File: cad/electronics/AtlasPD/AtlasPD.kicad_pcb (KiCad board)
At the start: 2 copper layers, 12 parts, among them J1 Conn_01x02_Male, J2 Conn_01x02_Male, U1 LM2678T-ADJ_NOPB

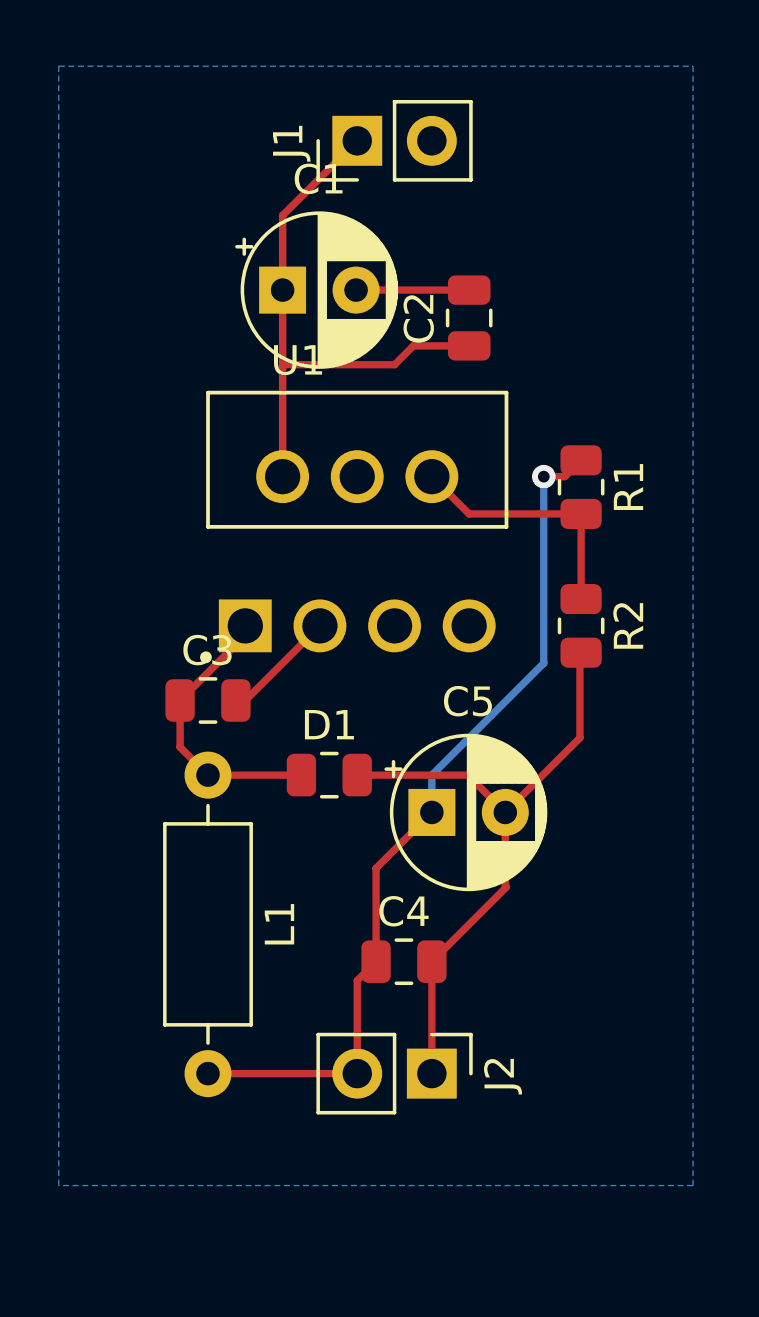
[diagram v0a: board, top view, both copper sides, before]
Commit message: Finished Basic Buck Converter Design
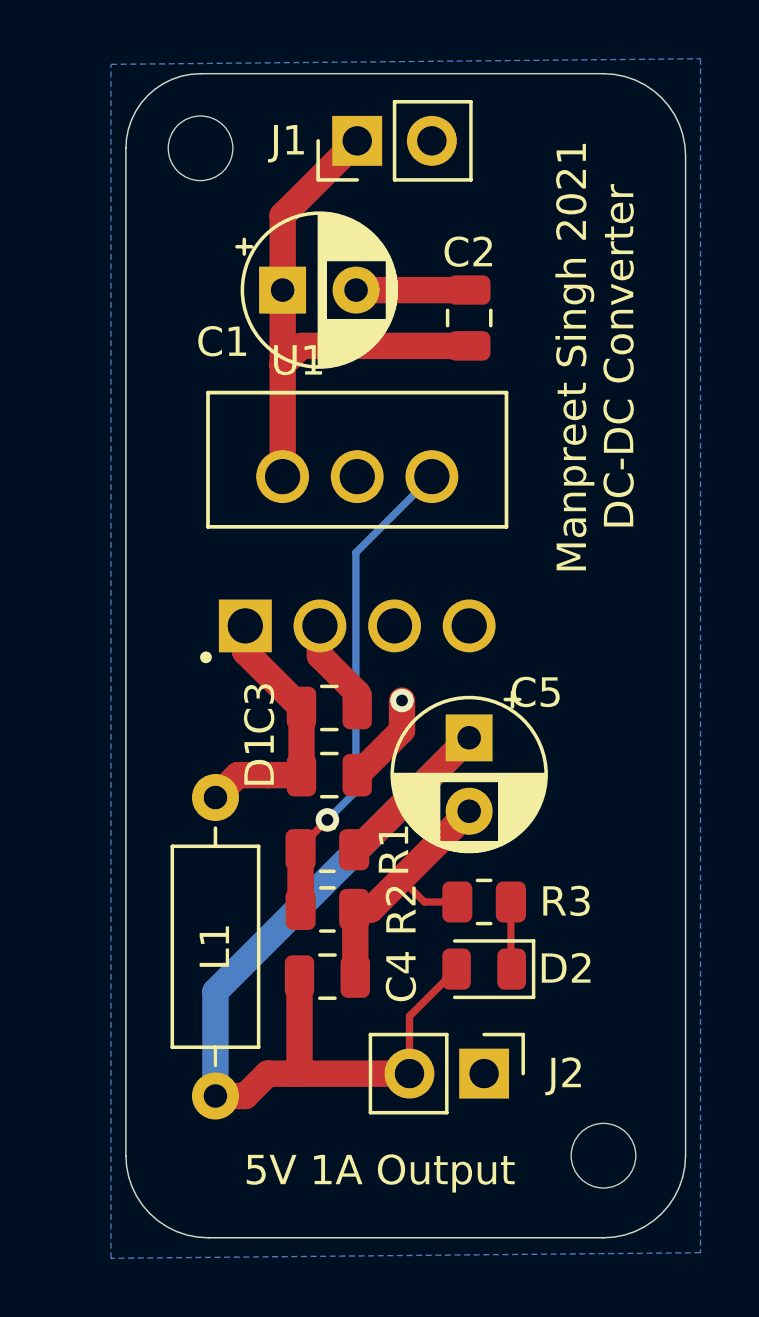
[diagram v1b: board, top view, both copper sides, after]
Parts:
- added D2: LED, LED_SMD:LED_0805_2012Metric, F.Cu at (42.4, 42.2)
- added R3: 1k, Resistor_SMD:R_0805_2012Metric, F.Cu at (42.4, 39.9)
- added REF**: MountingHole_2.2mm_M2_DIN965, MountingHole:MountingHole_2.2mm_M2_DIN965, F.Cu at (46.5, 48.5)
- added REF**: MountingHole_2.2mm_M2_DIN965, MountingHole:MountingHole_2.2mm_M2_DIN965, F.Cu at (32.8, 14.2)
- moved R1 15.1 mm to (37.1, 38.1), turned to 180 degrees
- moved R2 13.0 mm to (37.1, 40.1), turned to 0 degrees
- moved C3 4.14 mm to (37.1, 33.3)
- moved C5 2.84 mm to (41.9, 34.3), turned to 270 degrees
- moved C4 2.66 mm to (37.1, 42.4)
- moved J2 1.78 mm to (42.4, 45.7)
- moved L1 0.80 mm to (33.3, 36.3)
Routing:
- net GND: track 25.9 -> 16.8 mm, vias 0 -> 1
- net Net-(R1-Pad2): track 8.50 -> 16.6 mm, vias 0 -> 1
- net Net-(C4-Pad1): track 29.5 -> 35.7 mm, vias 1 -> 0
- net Net-(D2-Pad1): track 0.00 -> 2.30 mm
- net Net-(C3-Pad2): track 3.91 -> 3.32 mm
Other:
- board outline added: 19.1 x 39.6 mm
- board text added: "5V 1A Output"
- board text added: "Manpreet Singh 2021 DC-DC Converter"

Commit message: Pushing latest changes
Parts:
- added U2: NUCLEO-L432KC, NUCLEO-L432KC:MODULE_NUCLEO-L432KC, F.Cu at (80.5, 40.4)
- moved REF** 27.8 mm to (22.6, 34.3), turned to 270 degrees
- moved REF** 25.0 mm to (56.9, 20.6), turned to 270 degrees
- moved J2 23.0 mm to (25.4, 30.2), turned to 180 degrees
- moved J1 22.5 mm to (57.1, 25.9), turned to 0 degrees
- moved C4 19.4 mm to (28.7, 24.9), turned to 270 degrees
- moved D2 18.0 mm to (29.0, 30.2), turned to 90 degrees
- moved C1 17.1 mm to (52.1, 23.4), turned to 270 degrees
- moved R2 16.4 mm to (31.0, 24.9), turned to 270 degrees
- moved L1 15.3 mm to (34.8, 21.1), turned to 180 degrees
- moved R3 14.8 mm to (31.2, 30.2), turned to 90 degrees
- moved R1 13.8 mm to (33.0, 24.9), turned to 90 degrees
- moved C2 13.4 mm to (51.1, 29.7), turned to 0 degrees
- moved D1 10.7 mm to (35.6, 25.0), turned to 270 degrees
- moved C3 8.35 mm to (37.8, 25.0), turned to 270 degrees
- moved U1 7.64 mm to (45.7, 25.9), turned to 270 degrees
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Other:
- board size 19.1 x 39.6 mm -> 39.6 x 19.1 mm

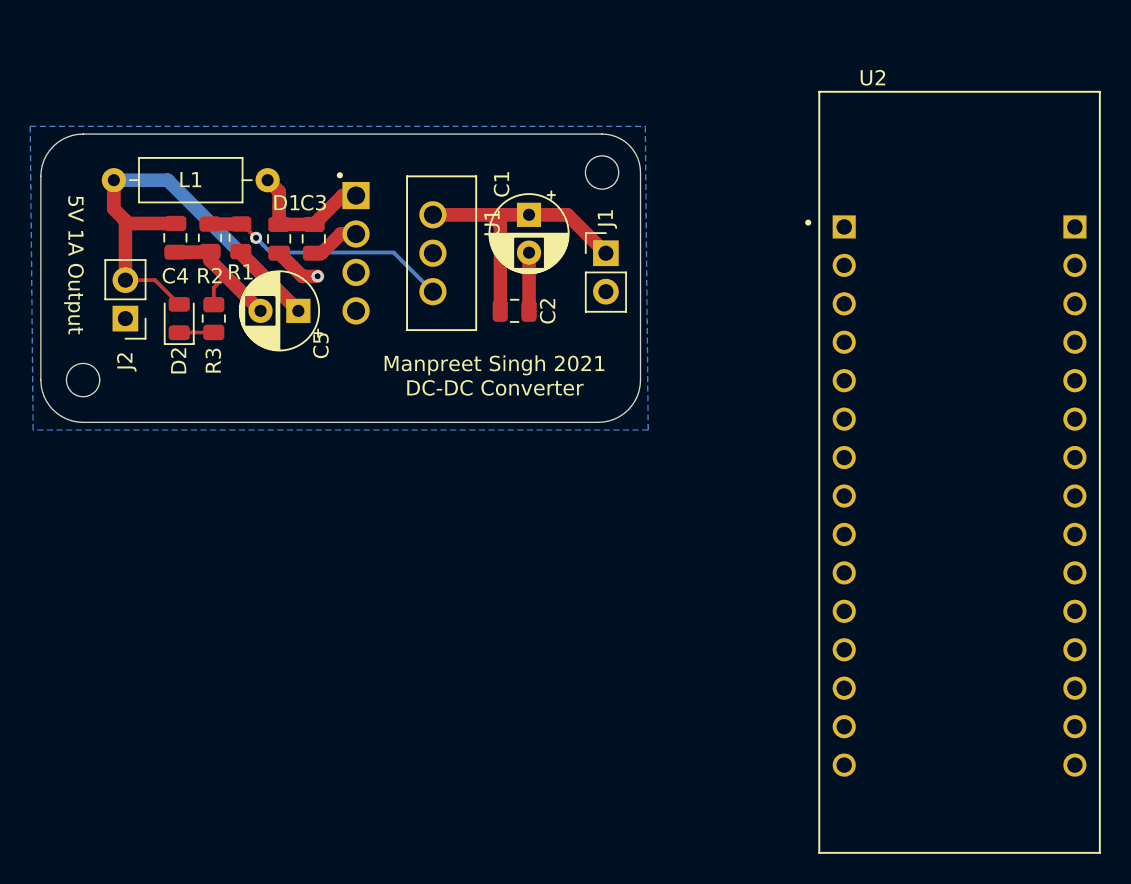
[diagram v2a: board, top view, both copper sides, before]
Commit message: PCB Changes to 5V Regulator
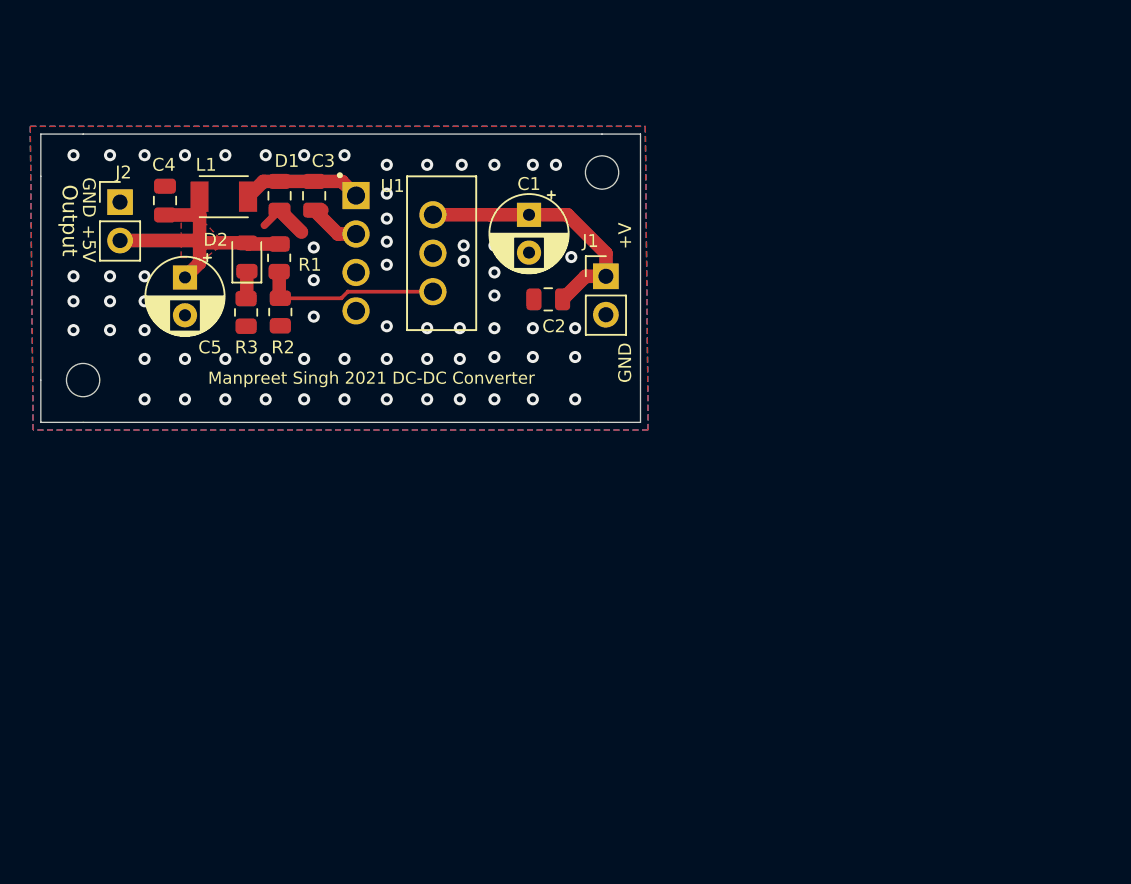
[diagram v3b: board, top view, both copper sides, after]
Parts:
- removed U2: NUCLEO-L432KC, NUCLEO-L432KC:MODULE_NUCLEO-L432KC
- L1: footprint Inductor_THT:L_Axial_L6.6mm_D2.7mm_P10.16mm_Horizontal_Vishay_IM-2 -> Inductor_SMD:L_TDK_NLV32_3.2x2.5mm
- moved C5 7.81 mm to (29.3, 27.5), turned to 270 degrees
- moved J2 7.70 mm to (25.0, 22.5), turned to 0 degrees
- moved R2 6.76 mm to (35.6, 29.8)
- moved D2 6.04 mm to (33.4, 26.2)
- moved L1 3.09 mm to (31.9, 22.2)
- moved R1 2.86 mm to (35.6, 26.2), turned to 270 degrees
- moved C3 2.84 mm to (37.9, 22.1)
- moved D1 2.84 mm to (35.6, 22.1)
- moved C4 2.56 mm to (28.0, 22.4), turned to 90 degrees
- moved C2 2.35 mm to (53.3, 29.0), turned to 180 degrees
- moved R3 2.17 mm to (33.4, 29.8), turned to 270 degrees
- moved J1 1.52 mm to (57.1, 27.4)
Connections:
- net Net-(C4-Pad1) renamed /Sheet60A23886/Output
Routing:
- net /Sheet60A23886/Output: track 35.7 -> 18.6 mm
- net GND: track 16.8 -> 3.47 mm, vias 1 -> 66
- net Net-(R1-Pad2): track 16.6 -> 12.1 mm, vias 1 -> 0
- net Net-(C1-Pad1): track 19.1 -> 17.5 mm
- net Net-(C3-Pad1): track 9.11 -> 7.94 mm
- net Net-(C3-Pad2): track 3.32 -> 3.93 mm
- added copper zone on F.Cu, net /Sheet60A23886/Output
- added copper zone on F.Cu, net GND
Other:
- outline, holes or cut-outs redrawn
- board text added: "+5V"
- board text added: "+V"
- board text added: "GND"
- board text added: "JLCJLCJLCJLC"
- board text added: "Output"
- board text removed: "5V 1A Output"

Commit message: More PCB changes
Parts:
- D1: footprint Capacitor_SMD:C_0805_2012Metric -> Diode_SMD:D_SOD-128
- moved D2 6.30 mm to (32.3, 32.4), turned to 180 degrees
- moved R3 3.74 mm to (36.1, 32.4), turned to 0 degrees
- moved L1 3.67 mm to (33.9, 25.2)
- moved C3 3.32 mm to (37.8, 25.4)
- moved R1 2.45 mm to (34.7, 28.5), turned to 0 degrees
- moved J2 2.28 mm to (27.0, 21.3)
- moved R2 2.26 mm to (37.8, 29.2)
- moved REF** 2.24 mm to (24.8, 34.3)
- moved C4 2.08 mm to (30.1, 22.1)
- moved C5 0.48 mm to (28.9, 27.5)
- moved D1 0.20 mm to (35.6, 21.9), turned to 180 degrees
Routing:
- net /Sheet60A23886/Output: track 18.6 -> 20.9 mm
- net Net-(R1-Pad2): track 12.1 -> 10.2 mm
- net GND: track 3.47 -> 2.56 mm, vias 66 -> 31
- removed copper zone on F.Cu, net /Sheet60A23886/Output
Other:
- board size 39.6 x 19.1 mm -> 37.4 x 19.1 mm

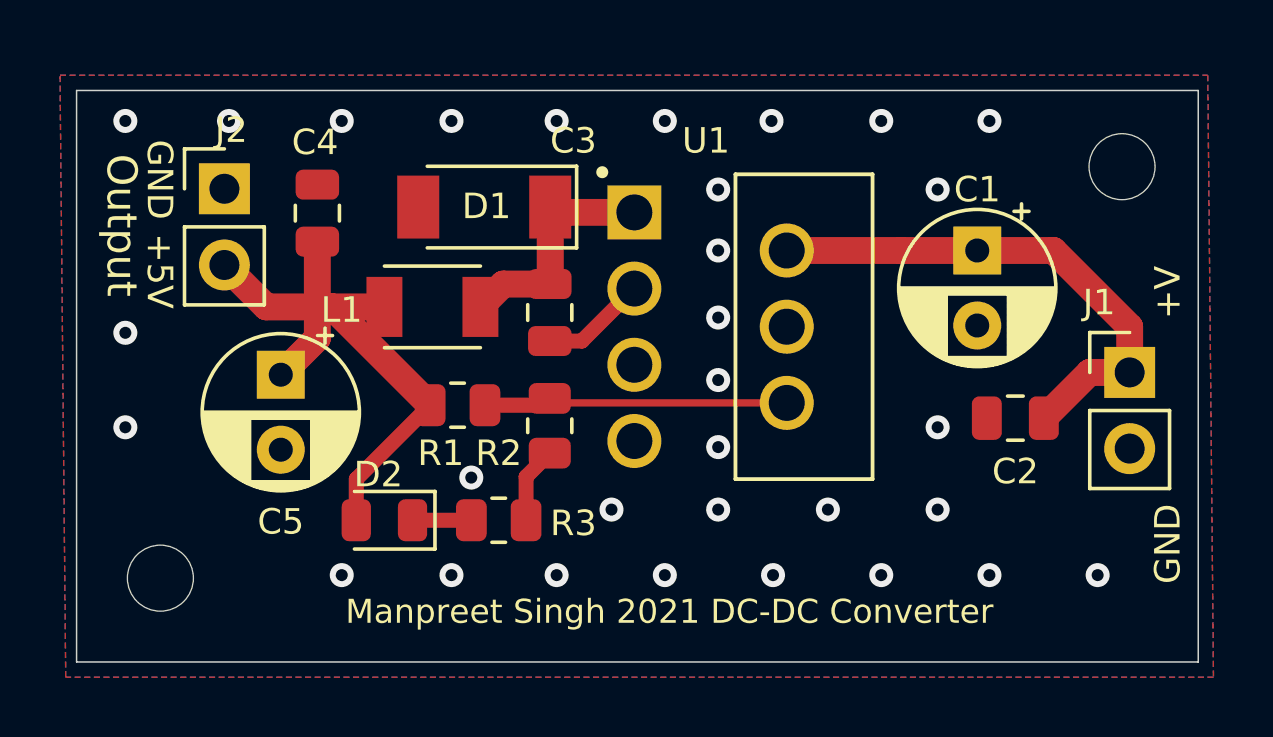
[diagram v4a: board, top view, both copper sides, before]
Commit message: Prep for short run production of power converter
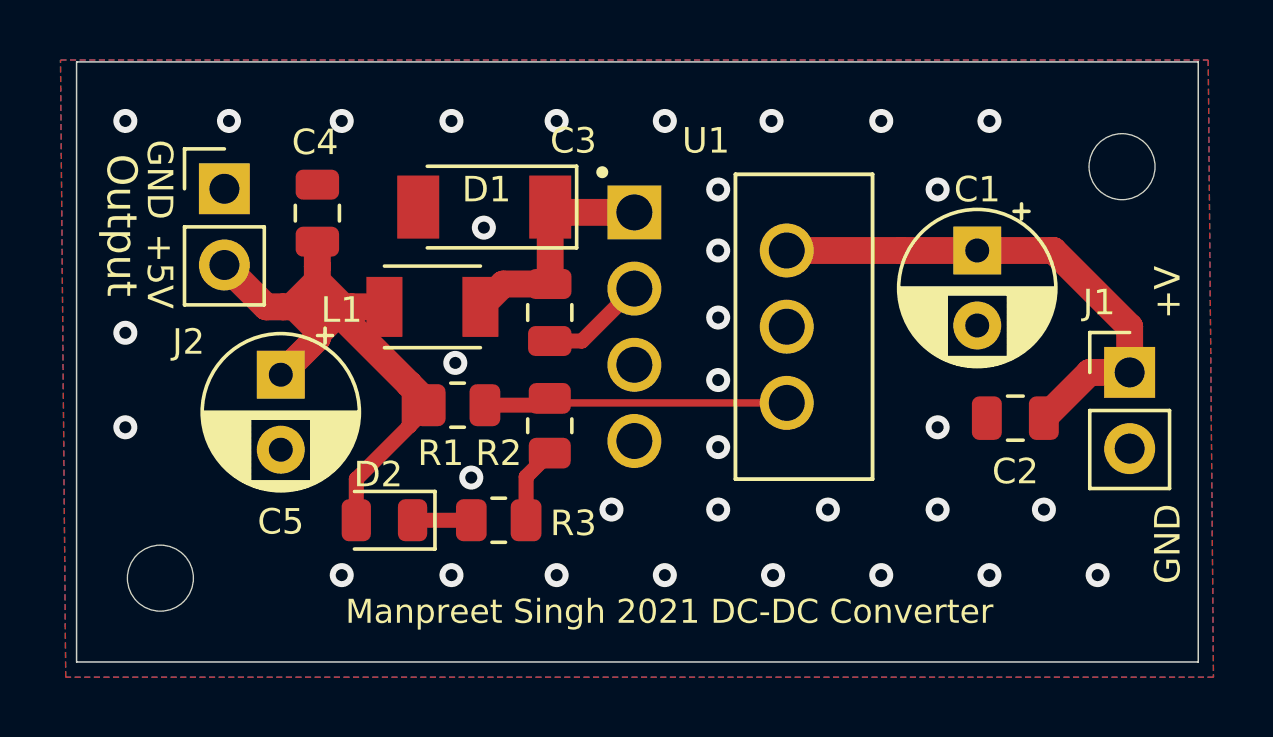
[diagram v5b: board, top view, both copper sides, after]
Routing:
- net /Sheet60A23886/Output: track 20.9 -> 28.4 mm
- net GND: vias 31 -> 34
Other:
- board size 37.4 x 19.1 mm -> 37.4 x 20 mm
